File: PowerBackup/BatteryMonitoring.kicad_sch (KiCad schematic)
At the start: 32 parts

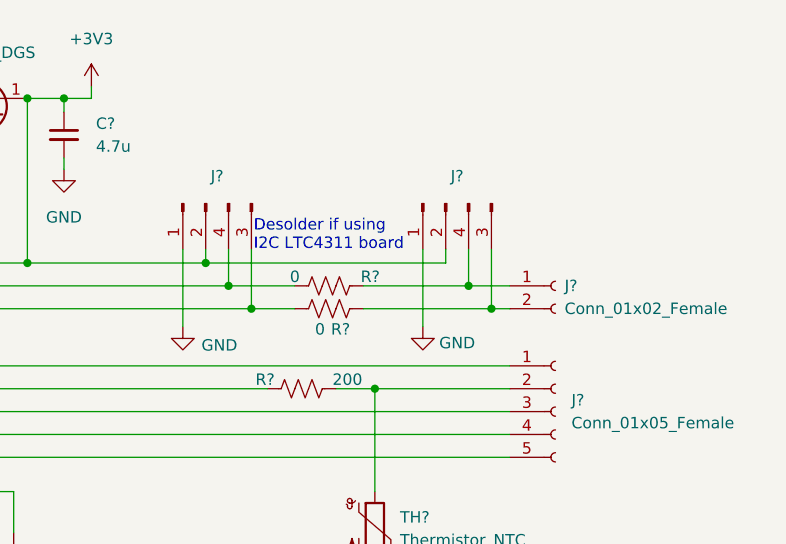
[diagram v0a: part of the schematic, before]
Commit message: Changed resistors and LEDs to 0805 and updated Production files
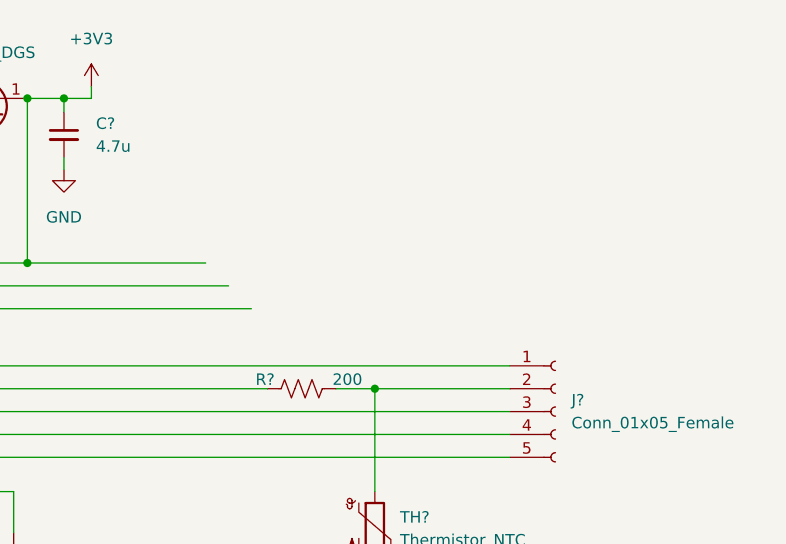
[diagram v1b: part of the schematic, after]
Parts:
- removed J?: Conn_01x02_Female, symbol Connector:Conn_01x02_Female
- removed J? (x2): Conn_01x04_Male, symbol Connector:Conn_01x04_Male
- removed R? (x2): 0, symbol Device:R_US
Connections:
- net at U?.9 (VC0): now also C?.1, R?.2
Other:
- note removed: "Desolder if using I2C LTC4311 board"
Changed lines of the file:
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@@
   (junction (at 172.212 57.658) (diameter 0) (color 0 0 0 0)
   )
-  (junction (at 187.96 75.946) (diameter 0) (color 0 0 0 0)
-  )
   (junction (at 168.148 75.946) (diameter 0) (color 0 0 0 0)
   )
@@
   (junction (at 78.74 92.456) (diameter 0) (color 0 0 0 0)
   )
-  (junction (at 190.5 78.486) (diameter 0) (color 0 0 0 0)
-  )
   (junction (at 94.234 100.33) (diameter 0) (color 0 0 0 0)
   )
-  (junction (at 217.17 78.486) (diameter 0) (color 0 0 0 0)
-  )
   (junction (at 147.574 121.158) (diameter 0) (color 0 0 0 0)
   )
@@
   (junction (at 117.602 100.33) (diameter 0) (color 0 0 0 0)
   )
-  (junction (at 219.71 81.026) (diameter 0) (color 0 0 0 0)
-  )
   (junction (at 127.762 62.23) (diameter 0) (color 0 0 0 0)
   )
@@
   (junction (at 109.728 100.33) (diameter 0) (color 0 0 0 0)
   )
-  (junction (at 193.04 81.026) (diameter 0) (color 0 0 0 0)
-  )
   (junction (at 109.728 82.296) (diameter 0) (color 0 0 0 0)
   )
@@
     (stroke (width 0) (type default) (color 0 0 0 0))
   )
-  (wire (pts (xy 217.17 78.486) (xy 217.17 74.422))
-    (stroke (width 0) (type default) (color 0 0 0 0))
-  )
   (wire (pts (xy 166.624 101.346) (xy 164.338 101.346))
     (stroke (width 0) (type default) (color 0 0 0 0))
@@
     (stroke (width 0) (type default) (color 0 0 0 0))
   )
-  (wire (pts (xy 190.5 78.486) (xy 190.5 74.422))
-    (stroke (width 0) (type default) (color 0 0 0 0))
-  )
   (wire (pts (xy 105.918 105.918) (xy 131.318 105.918))
     (stroke (width 0) (type default) (color 0 0 0 0))
@@
     (stroke (width 0) (type default) (color 0 0 0 0))
   )
-  (wire (pts (xy 205.486 81.026) (xy 219.71 81.026))
-    (stroke (width 0) (type default) (color 0 0 0 0))
-  )
   (wire (pts (xy 102.108 100.33) (xy 105.918 100.33))
     (stroke (width 0) (type default) (color 0 0 0 0))
@@
     (stroke (width 0) (type default) (color 0 0 0 0))
   )
-  (wire (pts (xy 185.42 74.422) (xy 185.42 83.058))
-    (stroke (width 0) (type default) (color 0 0 0 0))
-  )
   (wire (pts (xy 109.728 100.33) (xy 117.602 100.33))
     (stroke (width 0) (type default) (color 0 0 0 0))
   )
-  (wire (pts (xy 190.5 78.486) (xy 197.866 78.486))
-    (stroke (width 0) (type default) (color 0 0 0 0))
-  )
   (wire (pts (xy 105.918 100.33) (xy 105.918 105.918))
     (stroke (width 0) (type default) (color 0 0 0 0))
@@
     (stroke (width 0) (type default) (color 0 0 0 0))
   )
-  (wire (pts (xy 193.04 81.026) (xy 197.866 81.026))
-    (stroke (width 0) (type default) (color 0 0 0 0))
-  )
   (wire (pts (xy 94.234 87.376) (xy 138.938 87.376))
     (stroke (width 0) (type default) (color 0 0 0 0))
@@
     (stroke (width 0) (type default) (color 0 0 0 0))
   )
-  (wire (pts (xy 212.09 74.422) (xy 212.09 83.058))
-    (stroke (width 0) (type default) (color 0 0 0 0))
-  )
   (wire (pts (xy 58.928 92.456) (xy 59.436 92.456))
     (stroke (width 0) (type default) (color 0 0 0 0))
@@
     (stroke (width 0) (type default) (color 0 0 0 0))
   )
-  (wire (pts (xy 221.742 81.026) (xy 219.71 81.026))
-    (stroke (width 0) (type default) (color 0 0 0 0))
-  )
-  (wire (pts (xy 187.96 75.946) (xy 187.96 74.422))
-    (stroke (width 0) (type default) (color 0 0 0 0))
-  )
   (wire (pts (xy 164.338 89.916) (xy 194.818 89.916))
     (stroke (width 0) (type default) (color 0 0 0 0))
@@
     (stroke (width 0) (type default) (color 0 0 0 0))
   )
-  (wire (pts (xy 217.17 78.486) (xy 221.742 78.486))
-    (stroke (width 0) (type default) (color 0 0 0 0))
-  )
   (wire (pts (xy 86.614 89.916) (xy 138.938 89.916))
     (stroke (width 0) (type default) (color 0 0 0 0))
@@
     (stroke (width 0) (type default) (color 0 0 0 0))
   )
-  (wire (pts (xy 205.486 78.486) (xy 217.17 78.486))
-    (stroke (width 0) (type default) (color 0 0 0 0))
-  )
   (wire (pts (xy 154.178 66.04) (xy 154.178 67.056))
     (stroke (width 0) (type default) (color 0 0 0 0))
   )
-  (wire (pts (xy 214.63 75.946) (xy 214.63 74.422))
-    (stroke (width 0) (type default) (color 0 0 0 0))
-  )
   (wire (pts (xy 175.26 56.388) (xy 175.26 57.658))
     (stroke (width 0) (type default) (color 0 0 0 0))
@@
     (stroke (width 0) (type default) (color 0 0 0 0))
   )
-  (wire (pts (xy 193.04 81.026) (xy 193.04 74.422))
-    (stroke (width 0) (type default) (color 0 0 0 0))
-  )
-  (wire (pts (xy 219.71 74.422) (xy 219.71 81.026))
-    (stroke (width 0) (type default) (color 0 0 0 0))
-  )
   (wire (pts (xy 149.098 57.658) (xy 127.762 57.658))
     (stroke (width 0) (type default) (color 0 0 0 0))
@@
     (stroke (width 0) (type default) (color 0 0 0 0))
   )
-  (wire (pts (xy 187.96 75.946) (xy 214.63 75.946))
-    (stroke (width 0) (type default) (color 0 0 0 0))
-  )
   (wire (pts (xy 138.938 101.346) (xy 136.144 101.346))
     (stroke (width 0) (type default) (color 0 0 0 0))
   )
   (text "Replace with 200k\nif using PMOS\n" (at 137.922 57.15 0)
-    (effects (font (size 1.27 1.27)) (justify left bottom))
-  )
-  (text "Desolder if using \nI2C LTC4311 board\n" (at 193.294 74.676 0)
     (effects (font (size 1.27 1.27)) (justify left bottom))
   )
@@
     (pin "2")
   )
-  (symbol (lib_id "Connector:Conn_01x02_Female") (at 226.822 78.486 0) (unit 1)
-    (in_bom yes) (on_board yes) (fields_autoplaced)
-    (property "Reference" "J?" (id 0) (at 227.838 78.4859 0)
-      (effects (font (size 1.27 1.27)) (justify left))
-    )
-    (property "Value" "Conn_01x02_Female" (id 1) (at 227.838 81.0259 0)
-      (effects (font (size 1.27 1.27)) (justify left))
-    )
-    (property "Footprint" "" (id 2) (at 226.822 78.486 0)
-      (effects (font (size 1.27 1.27)) hide)
-    )
-    (property "Datasheet" "~" (id 3) (at 226.822 78.486 0)
-      (effects (font (size 1.27 1.27)) hide)
-    )
-    (pin "1")
-    (pin "2")
-  )
   (symbol (lib_id "Device:C_Small") (at 94.234 97.79 0) (unit 1)
     (in_bom yes) (on_board yes) (fields_autoplaced)
@@
     )
     (property "Datasheet" "~" (id 3) (at 94.234 97.79 0)
-      (effects (font (size 1.27 1.27)) hide)
-    )
-    (pin "1")
-    (pin "2")
-  )
-  (symbol (lib_id "Device:R_US") (at 201.676 78.486 270) (unit 1)
-    (in_bom yes) (on_board yes)
-    (property "Reference" "R?" (id 0) (at 206.248 77.47 90))
-    (property "Value" "0" (id 1) (at 197.866 77.47 90))
-    (property "Footprint" "" (id 2) (at 201.422 79.502 90)
-      (effects (font (size 1.27 1.27)) hide)
-    )
-    (property "Datasheet" "~" (id 3) (at 201.676 78.486 0)
       (effects (font (size 1.27 1.27)) hide)
     )
@@
     (pin "1")
     (pin "2")
-  )
-  (symbol (lib_id "Device:R_US") (at 201.676 81.026 270) (unit 1)
-    (in_bom yes) (on_board yes)
-    (property "Reference" "R?" (id 0) (at 202.946 83.312 90))
-    (property "Value" "0" (id 1) (at 200.66 83.312 90))
-    (property "Footprint" "" (id 2) (at 201.422 82.042 90)
-      (effects (font (size 1.27 1.27)) hide)
-    )
-    (property "Datasheet" "~" (id 3) (at 201.676 81.026 0)
-      (effects (font (size 1.27 1.27)) hide)
-    )
-    (pin "1")
-    (pin "2")
-  )
-  (symbol (lib_name "Conn_01x04_Male_1") (lib_id "Connector:Conn_01x04_Male") (at 187.96 69.342 90) (mirror x) (unit 1)
-    (in_bom yes) (on_board yes) (fields_autoplaced)
-    (property "Reference" "J?" (id 0) (at 189.23 66.294 90))
-    (property "Value" "Conn_01x04_Male" (id 1) (at 184.912 70.612 90)
-      (effects (font (size 1.27 1.27)) hide)
-    )
-    (property "Footprint" "" (id 2) (at 187.96 69.342 0)
-      (effects (font (size 1.27 1.27)) hide)
-    )
-    (property "Datasheet" "~" (id 3) (at 187.96 69.342 0)
-      (effects (font (size 1.27 1.27)) hide)
-    )
-    (pin "1")
-    (pin "2")
-    (pin "4")
-    (pin "3")
-  )
-  (symbol (lib_name "Conn_01x04_Male_1") (lib_id "Connector:Conn_01x04_Male") (at 214.63 69.342 90) (mirror x) (unit 1)
-    (in_bom yes) (on_board yes) (fields_autoplaced)
-    (property "Reference" "J?" (id 0) (at 215.9 66.294 90))
-    (property "Value" "Conn_01x04_Male" (id 1) (at 211.582 70.612 90)
-      (effects (font (size 1.27 1.27)) hide)
-    )
-    (property "Footprint" "" (id 2) (at 214.63 69.342 0)
-      (effects (font (size 1.27 1.27)) hide)
-    )
-    (property "Datasheet" "~" (id 3) (at 214.63 69.342 0)
-      (effects (font (size 1.27 1.27)) hide)
-    )
-    (pin "1")
-    (pin "2")
-    (pin "3")
-    (pin "4")
   )
   (symbol (lib_id "Device:R_US") (at 65.532 92.456 90) (unit 1)
@@
     (pin "1")
     (pin "2")
-  )
-  (symbol (lib_id "power:GND") (at 185.42 83.058 0) (unit 1)
-    (in_bom yes) (on_board yes)
-    (property "Reference" "#PWR?" (id 0) (at 185.42 89.408 0)
-      (effects (font (size 1.27 1.27)) hide)
-    )
-    (property "Value" "GND" (id 1) (at 189.484 85.09 0))
-    (property "Footprint" "" (id 2) (at 185.42 83.058 0)
-      (effects (font (size 1.27 1.27)) hide)
-    )
-    (property "Datasheet" "" (id 3) (at 185.42 83.058 0)
-      (effects (font (size 1.27 1.27)) hide)
-    )
-    (pin "1")
   )
   (symbol (lib_id "Device:Q_PMOS_DGS") (at 163.068 60.198 270) (mirror x) (unit 1)
@@
     (pin "3")
   )
-  (symbol (lib_id "power:GND") (at 212.09 83.058 0) (unit 1)
-    (in_bom yes) (on_board yes)
-    (property "Reference" "#PWR?" (id 0) (at 212.09 89.408 0)
-      (effects (font (size 1.27 1.27)) hide)
-    )
-    (property "Value" "GND" (id 1) (at 215.9 84.836 0))
-    (property "Footprint" "" (id 2) (at 212.09 83.058 0)
-      (effects (font (size 1.27 1.27)) hide)
-    )
-    (property "Datasheet" "" (id 3) (at 212.09 83.058 0)
-      (effects (font (size 1.27 1.27)) hide)
-    )
-    (pin "1")
-  )
 )

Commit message: Did some initial board layout
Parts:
- removed Q?: Q_PMOS_DGS, symbol Device:Q_PMOS_DGS
- added J3, J5: Conn_01x04_Male, symbol Connector:Conn_01x04_Male
- added J6: Conn_01x02_Female, Connector_JST:JST_XH_B2B-XH-A_1x02_P2.50mm_Vertical, symbol Connector:Conn_01x02_Female
- added Q1: ZXTP25040DFH, Package_TO_SOT_SMD:SOT-23, symbol Device:Q_PNP_BEC
- added R13, R15: 4k7, Resistor_SMD:R_0805_2012Metric, symbol Device:R_US
- added R16, R17: 0, Resistor_SMD:R_0805_2012Metric, symbol Device:R_US
- C1, C2, C3, C4, C5, C6, C7, C8, C9: renamed from C?; footprint (none) -> Capacitor_SMD:C_0805_2012Metric
- J2: renamed from J?; footprint (none) -> Connector_JST:JST_XH_B7B-XH-A_1x07_P2.50mm_Vertical
- J4: renamed from J?; footprint (none) -> Connector_PinHeader_1.00mm:PinHeader_1x05_P1.00mm_Vertical_SMD_Pin1Left
- R1, R10, R11, R14, R2, R3, R4, R5, R6, R7, R8: renamed from R?; footprint (none) -> Resistor_SMD:R_0805_2012Metric
- R12, R9: renamed from R?; value R_US -> 1k; footprint (none) -> Resistor_SMD:R_0805_2012Metric
- TH1: renamed from TH?; footprint (none) -> Resistor_SMD:R_0805_2012Metric
- gave numbers to parts that had none: 1
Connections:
- net +3V3: now also J3.2 (Pin_2), J5.2 (Pin_2), Q1.3 (C), R13.2, R15.2
- net GNDD: now also J3.1 (Pin_1), J5.1 (Pin_1)
- net at C8.1, R11.2, R8.2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: now also Q1.2 (E)
- net at R11.1, U1.1 (VCTL): now also Q1.1 (B)
- net at U1.18 (SDA): now also J3.3 (Pin_4), R15.1, R17.2
- net at U1.19 (SCL): now also J3.4 (Pin_3), R13.1, R16.2
- net at U1.9 (VC0): now also C1.1, R4.2
- new net: J5.4 (Pin_3), J6.1 (Pin_1), R16.1
- new net: J5.3 (Pin_4), J6.2 (Pin_2), R17.1
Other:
- note added: "DESIGN NOTE: Device 7-bit Adress BQ76925 0b100XXXX"
- note added: "Desolder if using I2C LTC4311 board"
- moved on the sheet: C1, C2, C3, C4, C5, C6, C7, C8, C9, J2, J4, R1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

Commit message: Trying things
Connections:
- net GNDD is gone; now on net GND: J3.1 (Pin_1), J5.1 (Pin_1), R10.2, R12.2
- net at U1.9 (VC0): now also C1.1, R4.2
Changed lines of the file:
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@@
     (pin "2")
-  )
-  (symbol (lib_id "power:GNDD") (at 235.458 88.392 0) (unit 1)
-    (in_bom yes) (on_board yes)
-    (property "Reference" "#PWR0109" (id 0) (at 235.458 94.742 0)
-      (effects (font (size 1.27 1.27)) hide)
-    )
-    (property "Value" "GNDD" (id 1) (at 238.506 88.9 0))
-    (property "Footprint" "" (id 2) (at 235.458 88.392 0)
-      (effects (font (size 1.27 1.27)) hide)
-    )
-    (property "Datasheet" "" (id 3) (at 235.458 88.392 0)
-      (effects (font (size 1.27 1.27)) hide)
-    )
-    (pin "1")
   )
   (symbol (lib_id "power:+3V3") (at 165.354 61.722 0) (unit 1)
@@
     (pin "2")
   )
+  (symbol (lib_id "power:GND") (at 145.288 129.286 0) (unit 1)
+    (in_bom yes) (on_board yes) (fields_autoplaced)
+    (property "Reference" "#PWR05" (id 0) (at 145.288 135.636 0)
+      (effects (font (size 1.27 1.27)) hide)
+    )
+    (property "Value" "GND" (id 1) (at 145.288 134.112 0))
+    (property "Footprint" "" (id 2) (at 145.288 129.286 0)
+      (effects (font (size 1.27 1.27)) hide)
+    )
+    (property "Datasheet" "" (id 3) (at 145.288 129.286 0)
+      (effects (font (size 1.27 1.27)) hide)
+    )
+    (pin "1")
+  )
   (symbol (lib_id "Device:R_US") (at 193.294 74.676 180) (unit 1)
     (in_bom yes) (on_board yes)
@@
     (pin "2")
   )
+  (symbol (lib_id "power:GND") (at 208.788 88.392 0) (unit 1)
+    (in_bom yes) (on_board yes) (fields_autoplaced)
+    (property "Reference" "#PWR06" (id 0) (at 208.788 94.742 0)
+      (effects (font (size 1.27 1.27)) hide)
+    )
+    (property "Value" "GND" (id 1) (at 208.788 93.726 0))
+    (property "Footprint" "" (id 2) (at 208.788 88.392 0)
+      (effects (font (size 1.27 1.27)) hide)
+    )
+    (property "Datasheet" "" (id 3) (at 208.788 88.392 0)
+      (effects (font (size 1.27 1.27)) hide)
+    )
+    (pin "1")
+  )
   (symbol (lib_id "power:GND") (at 137.668 129.286 0) (unit 1)
     (in_bom yes) (on_board yes) (fields_autoplaced)
@@
     )
     (property "Datasheet" "" (id 3) (at 196.85 115.062 0)
+      (effects (font (size 1.27 1.27)) hide)
+    )
+    (pin "1")
+  )
+  (symbol (lib_id "power:GND") (at 235.458 88.392 0) (unit 1)
+    (in_bom yes) (on_board yes) (fields_autoplaced)
+    (property "Reference" "#PWR07" (id 0) (at 235.458 94.742 0)
+      (effects (font (size 1.27 1.27)) hide)
+    )
+    (property "Value" "GND" (id 1) (at 235.458 93.726 0))
+    (property "Footprint" "" (id 2) (at 235.458 88.392 0)
+      (effects (font (size 1.27 1.27)) hide)
+    )
+    (property "Datasheet" "" (id 3) (at 235.458 88.392 0)
       (effects (font (size 1.27 1.27)) hide)
     )
@@
     (pin "2")
   )
-  (symbol (lib_id "power:GNDD") (at 208.788 88.392 0) (unit 1)
-    (in_bom yes) (on_board yes)
-    (property "Reference" "#PWR0108" (id 0) (at 208.788 94.742 0)
-      (effects (font (size 1.27 1.27)) hide)
-    )
-    (property "Value" "GNDD" (id 1) (at 211.836 88.9 0))
-    (property "Footprint" "" (id 2) (at 208.788 88.392 0)
-      (effects (font (size 1.27 1.27)) hide)
-    )
-    (property "Datasheet" "" (id 3) (at 208.788 88.392 0)
-      (effects (font (size 1.27 1.27)) hide)
-    )
-    (pin "1")
-  )
   (symbol (lib_id "Device:C_Small") (at 162.306 67.056 0) (unit 1)
     (in_bom yes) (on_board yes) (fields_autoplaced)
@@
     (pin "5")
   )
-  (symbol (lib_id "power:GNDD") (at 145.288 129.286 0) (unit 1)
-    (in_bom yes) (on_board yes) (fields_autoplaced)
-    (property "Reference" "#PWR0107" (id 0) (at 145.288 135.636 0)
-      (effects (font (size 1.27 1.27)) hide)
-    )
-    (property "Value" "GNDD" (id 1) (at 145.288 134.112 0))
-    (property "Footprint" "" (id 2) (at 145.288 129.286 0)
-      (effects (font (size 1.27 1.27)) hide)
-    )
-    (property "Datasheet" "" (id 3) (at 145.288 129.286 0)
-      (effects (font (size 1.27 1.27)) hide)
-    )
-    (pin "1")
-  )
   (symbol (lib_name "Conn_01x04_Male_1") (lib_id "Connector:Conn_01x04_Male") (at 237.998 74.676 90) (mirror x) (unit 1)

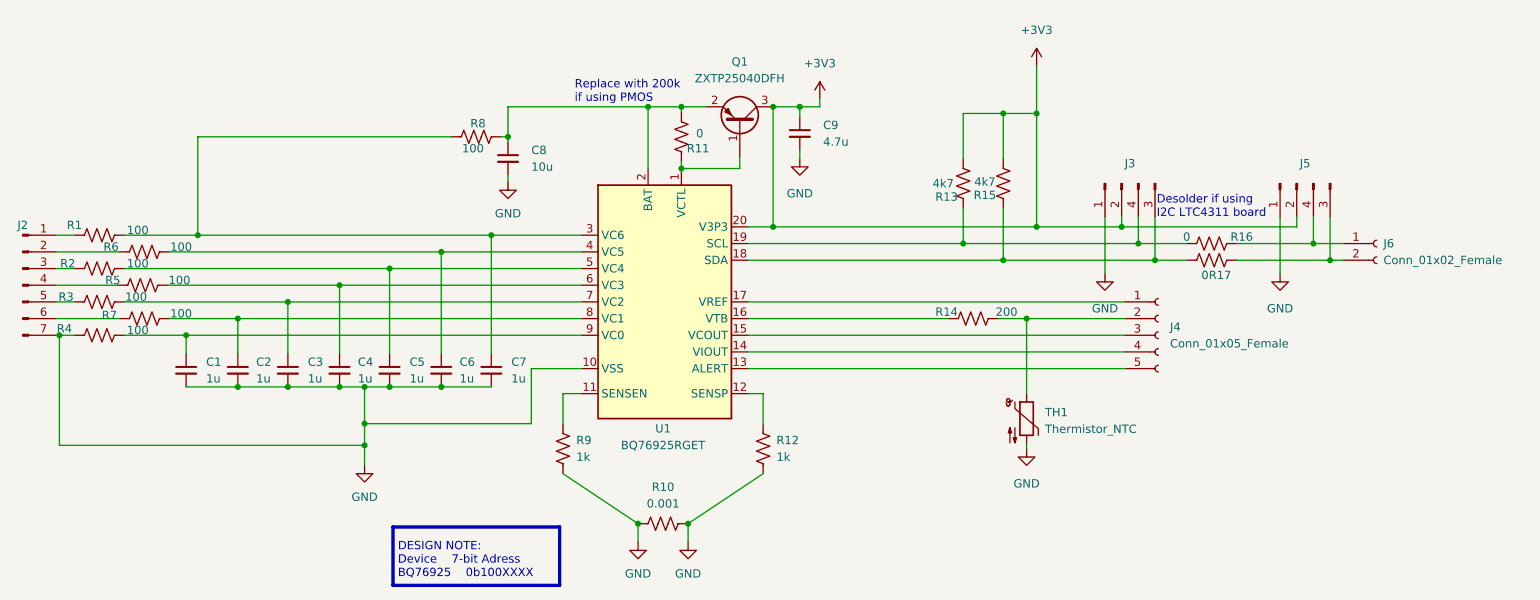
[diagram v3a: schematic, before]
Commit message: Adding regulator
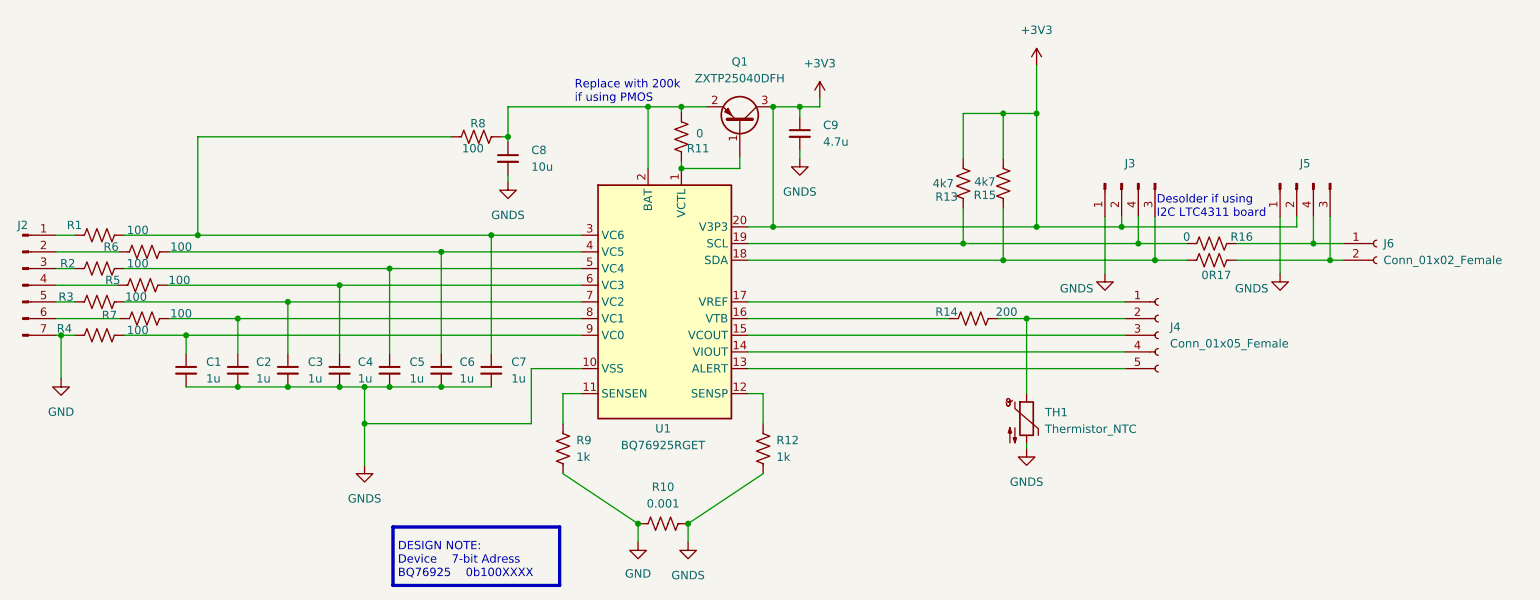
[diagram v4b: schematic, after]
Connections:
- net GND: no longer C1.2, C2.2, C3.2, C4.2, C5.2, C6.2, C7.2, C8.2, C9.2, J3.1 (Pin_1), J5.1 (Pin_1), R10.2, R12.2, TH1.2, U1.10 (VSS)
- net GNDS: now reaches U1.10 (VSS)
- net GNDS: now also C1.2, C2.2, C3.2, C4.2, C5.2, C6.2, C7.2, C8.2, C9.2, J3.1 (Pin_1), J5.1 (Pin_1), R10.2, R12.2, TH1.2
- net at U1.9 (VC0): now also C1.1, R4.2
